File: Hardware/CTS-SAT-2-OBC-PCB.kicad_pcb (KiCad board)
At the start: 6 copper layers, 95.9 x 90.2 mm, 209 parts, among them IC1 STTS22HTR, IC2 MT29F1G01ABAFDSF-AAT_F_TR, IC3 MT29F1G01ABAFDSF-AAT_F_TR, IC4 MT29F1G01ABAFDSF-AAT_F_TR, IC5 MT29F1G01ABAFDSF-AAT_F_TR, J1 J-0530471010, J10 J-0532610871, J11 J-TSW-106-05-T-S, J12 J-0532610671, J13 J-0532610471, J14 J-0532610471, J15 J-TSW-106-05-T-S, J16 J-0532610671, J18 252105, J19 252105, J2 2-Pin Header, J20 252105, J21 J-0530471010, J22 J-0530471010, J23 J-0532610471, J24 USB_C_Receptacle_USB2.0_14P, J25 J-0532610471, J3 ESQ-126-14-G-D, J4 ESQ-126-14-G-D, J5 2-Pin Header, J6 2-Pin Header, J7 J-0532610671, J8 J-0532610471, J9 J-0532610871, SW1 SW_Push_Dual, SW2 SW_Push_Dual, U1 W25Q128JVS, U2 RP2040, U3 STM32L4R5ZITx, U4 SN74LVC1G14DCKR, U5 HMC544AE, U6 U-MAX3378EEUD+T, U7 MAX3086EESD+T, Y1 ABM8-272-T3, Y2 TG-3541CE_32.7680KXB3, Y3 ECS-TXO-2520-33-250-AN-TR

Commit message: Update schematic to allow using STM32 alone
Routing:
- removed copper zone on In3.Cu, net +3V3
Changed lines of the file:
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@@
 		(min_thickness 0.25)
 		(filled_areas_thickness no)
-		(fill
+		(fill yes
 			(thermal_gap 0.5)
 			(thermal_bridge_width 0.5)
@@
 			)
 		)
-	)
-	(zone
-		(net 8)
-		(net_name "+3V3")
-		(layer "In3.Cu")
-		(hatch edge 0.5)
-		(connect_pads
-			(clearance 0.5)
-		)
-		(min_thickness 0.25)
-		(filled_areas_thickness no)
-		(fill
-			(thermal_gap 0.5)
-			(thermal_bridge_width 0.5)
-		)
-		(polygon
-			(pts
-				(xy 98.247834 56.66535) (xy 190.247834 56.66535) (xy 190.247834 114.592668) (xy 98.247834 126.342668)
-			)
-		)

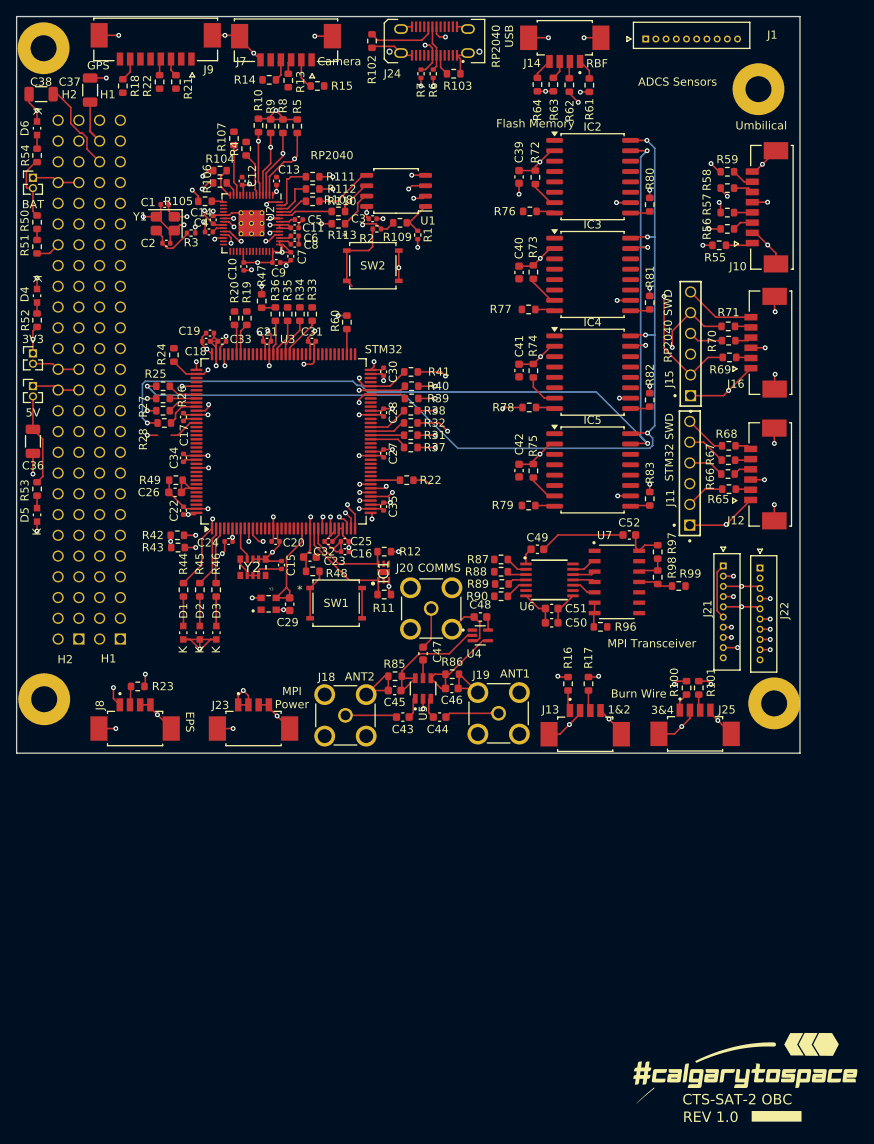
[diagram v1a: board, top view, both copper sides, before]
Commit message: Adjust Comms layout
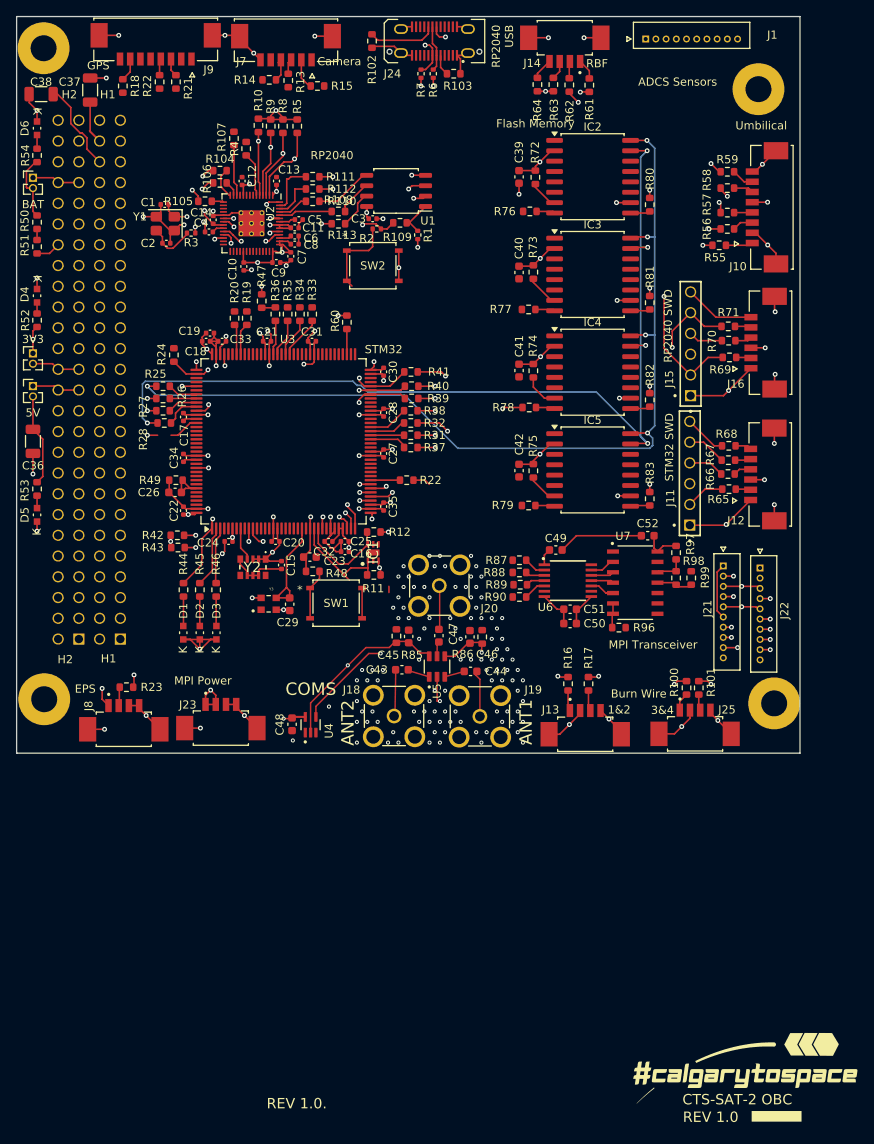
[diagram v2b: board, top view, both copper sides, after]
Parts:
- moved C48 26.5 mm to (133.7, 136.6), turned to 90 degrees
- moved U4 23.5 mm to (136.0, 136.7), turned to 90 degrees
- moved C45 6.83 mm to (148.0, 125.9), turned to 90 degrees
- moved C44 6.75 mm to (155.6, 130.2)
- moved C46 6.69 mm to (155.5, 125.9), turned to -90 degrees
- moved J18 5.95 mm to (146.2, 135.6)
- moved R86 5.85 mm to (157.0, 125.9), turned to -90 degrees
- moved C43 5.79 mm to (147.2, 130.0)
- moved R85 4.92 mm to (146.5, 125.8), turned to 90 degrees
- moved J23 4.00 mm to (125.0, 134.2)
- moved U5 3.18 mm to (151.5, 129.6)
- moved J20 2.97 mm to (151.7, 119.7)
- moved C47 2.93 mm to (151.7, 125.8)
- moved IC1 2.72 mm to (143.7, 115.6)
- moved R11 2.72 mm to (143.7, 118.3)
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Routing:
- net GND: track 264.5 -> 243.1 mm, vias 63 -> 166
- net /Antenna/N_UHF_CTRL: track 13.0 -> 18.4 mm, vias 0 -> 2
- net /Antenna/UHF_CTRL: track 17.0 -> 22.2 mm, vias 0 -> 1
- net /Connectors/MISO_UART5_RX: track 40.6 -> 38.0 mm
- net Net-(C44-Pad1): track 6.99 -> 5.72 mm
- net +3V3: track 134.0 -> 135.2 mm, vias 39 -> 40
- net 3V3: track 6.10 -> 6.96 mm, vias 0 -> 1
- net Net-(C43-Pad1): track 6.34 -> 5.65 mm
- net Net-(C47-Pad2): track 5.15 -> 5.71 mm
- net Net-(U5-RFC): track 2.60 -> 2.06 mm
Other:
- board text added: "COMS"
- board text added: "REV 1.0."
- board text removed: "COMMS"

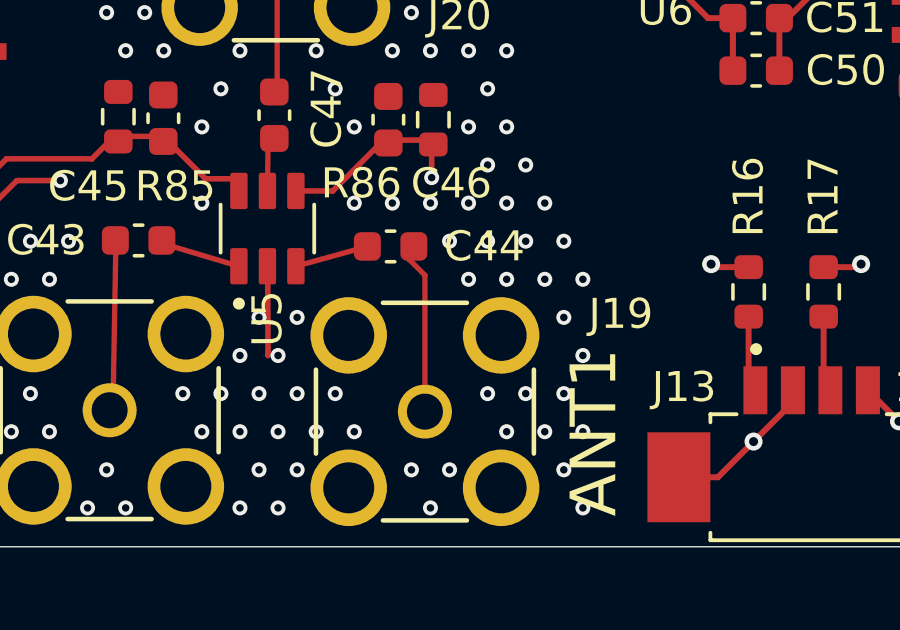
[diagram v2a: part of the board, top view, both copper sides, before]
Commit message: minor routing change for comms
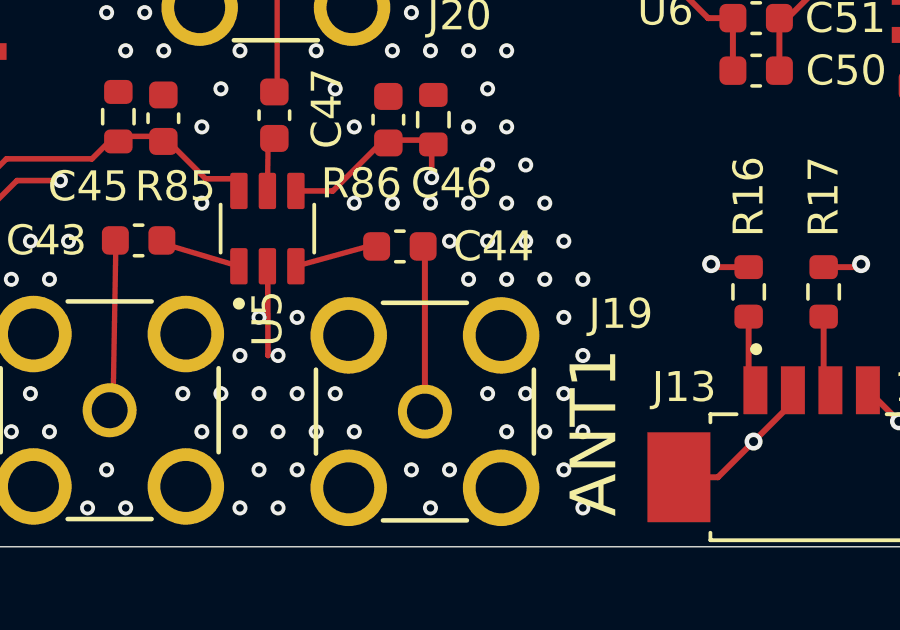
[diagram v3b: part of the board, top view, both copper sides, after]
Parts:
- moved C44 0.31 mm to (155.9, 130.2)

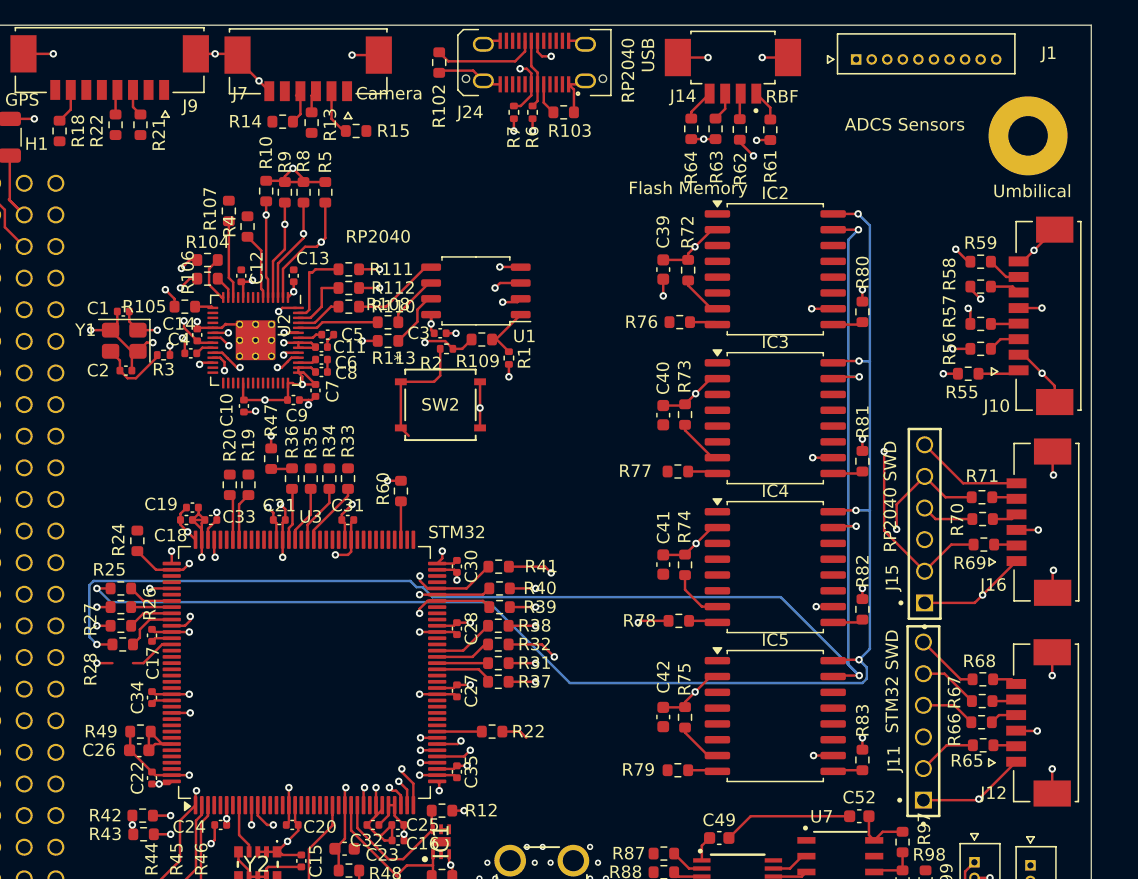
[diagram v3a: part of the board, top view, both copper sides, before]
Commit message: Populate more resistors
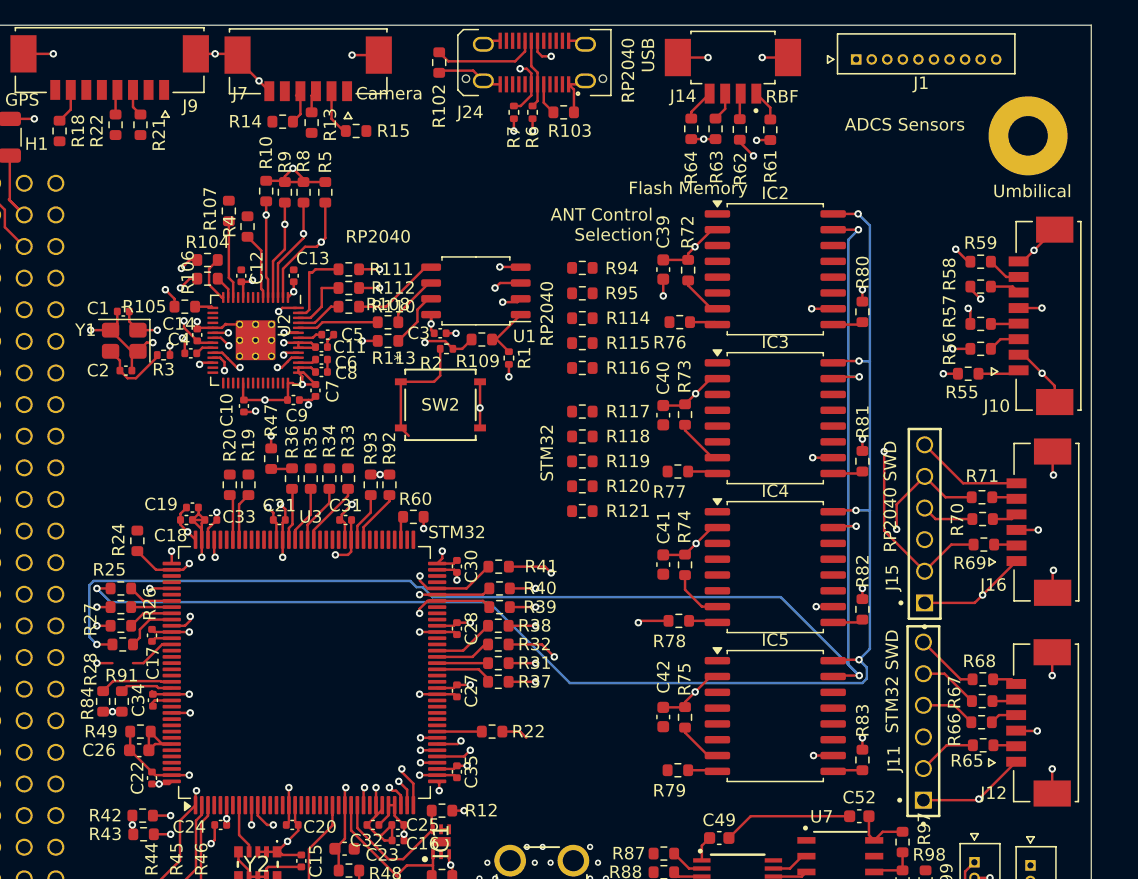
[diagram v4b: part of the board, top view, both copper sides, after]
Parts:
- added R114: 0R, Resistor_SMD:R_0603_1608Metric, F.Cu at (155.0, 73.5)
- added R115: 0R, Resistor_SMD:R_0603_1608Metric, F.Cu at (155.0, 75.5)
- added R116: 0R, Resistor_SMD:R_0603_1608Metric, F.Cu at (155.0, 77.5)
- added R117: 0R, Resistor_SMD:R_0603_1608Metric, F.Cu at (155.0, 81.0)
- added R118: 0R, Resistor_SMD:R_0603_1608Metric, F.Cu at (155.0, 83.0)
- added R119: 0R, Resistor_SMD:R_0603_1608Metric, F.Cu at (155.0, 85.0)
- added R120: 0R, Resistor_SMD:R_0603_1608Metric, F.Cu at (155.0, 87.0)
- added R121: 0R, Resistor_SMD:R_0603_1608Metric, F.Cu at (155.0, 89.0)
- added R84: 4k7, Resistor_SMD:R_0603_1608Metric, F.Cu at (116.5, 104.3)
- added R91: 4k7, Resistor_SMD:R_0603_1608Metric, F.Cu at (118.0, 104.3)
- added R92: 4k7, Resistor_SMD:R_0603_1608Metric, F.Cu at (139.5, 86.9)
- added R93: 4k7, Resistor_SMD:R_0603_1608Metric, F.Cu at (138.0, 86.9)
- added R94: 0R, Resistor_SMD:R_0603_1608Metric, F.Cu at (155.0, 69.5)
- added R95: 0R, Resistor_SMD:R_0603_1608Metric, F.Cu at (155.0, 71.5)
- moved R60 2.30 mm to (141.4, 89.5), turned to 0 degrees
- moved C34 0.22 mm to (120.5, 104.2)
- moved C31 0.18 mm to (136.0, 89.8)
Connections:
- R10 pad 2: /Antenna/ANT_I2C1_SCL -> /RP2040/I2C1_SCL
- R4 pad 2: /Antenna/UHF_CTRL -> /RP2040/UHF_CTL
- R5 pad 2: /Antenna/ANT_I2C0_SDA -> /RP2040/I2C0_SDA
- R8 pad 2: /Antenna/ANT_I2C0_SCL -> /RP2040/I2C0_SCL
- R9 pad 2: /Antenna/ANT_I2C1_SDA -> /RP2040/I2C1_SDA
- U2 pad 2: /Antenna/ANT_I2C0_SDA -> /RP2040/I2C0_SDA
- U2 pad 3: /Antenna/ANT_I2C0_SCL -> /RP2040/I2C0_SCL
- U2 pad 4: /Antenna/ANT_I2C1_SDA -> /RP2040/I2C1_SDA
- U2 pad 5: /Antenna/ANT_I2C1_SCL -> /RP2040/I2C1_SCL
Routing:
- net /RP2040/I2C0_SDA: track 0.00 -> 9.57 mm, vias 0 -> 1
- net /Antenna/ANT_I2C0_SDA: track 10.8 -> 1.25 mm, vias 2 -> 1
- net /RP2040/I2C0_SCL: track 0.00 -> 8.47 mm, vias 0 -> 1
- net /Antenna/ANT_I2C0_SCL: track 9.47 -> 1.00 mm, vias 2 -> 1
- net /RP2040/I2C1_SDA: track 0.00 -> 8.02 mm, vias 0 -> 1
- net /Antenna/ANT_I2C1_SDA: track 9.27 -> 1.25 mm, vias 2 -> 1
- net /RP2040/I2C1_SCL: track 0.00 -> 7.79 mm, vias 0 -> 1
- net /Antenna/ANT_I2C1_SCL: track 8.79 -> 1.00 mm, vias 2 -> 1
- net /Connectors/MISO_USART2_RX: track 6.54 -> 0.00 mm, vias 1 -> 0
- net (no net): track 0.00 -> 6.54 mm, vias 0 -> 1
- net /STM32/I2C1_SDA: track 0.00 -> 5.87 mm
- net /STM32/I2C4_SCL: track 0.00 -> 4.45 mm
- net /STM32/I2C1_SCL: track 0.00 -> 4.24 mm
- net /STM32/I2C4_SDA: track 0.00 -> 4.03 mm
- net +3V3: track 135.2 -> 138.0 mm, vias 40 -> 42
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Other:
- board text added: "ANT Control Selection"
